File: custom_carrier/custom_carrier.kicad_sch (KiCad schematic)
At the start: 20 parts, among them J1 ERF5-040-05.0-X-DV, J13 PJ-002AH-SMT-TR, J14 87832-1420, J2 ERF5-040-05.0-X-DV, J3 ERF5-040-05.0-X-DV, J4 ERF5-040-05.0-X-DV, J5 45230-220230, J6 45230-220230

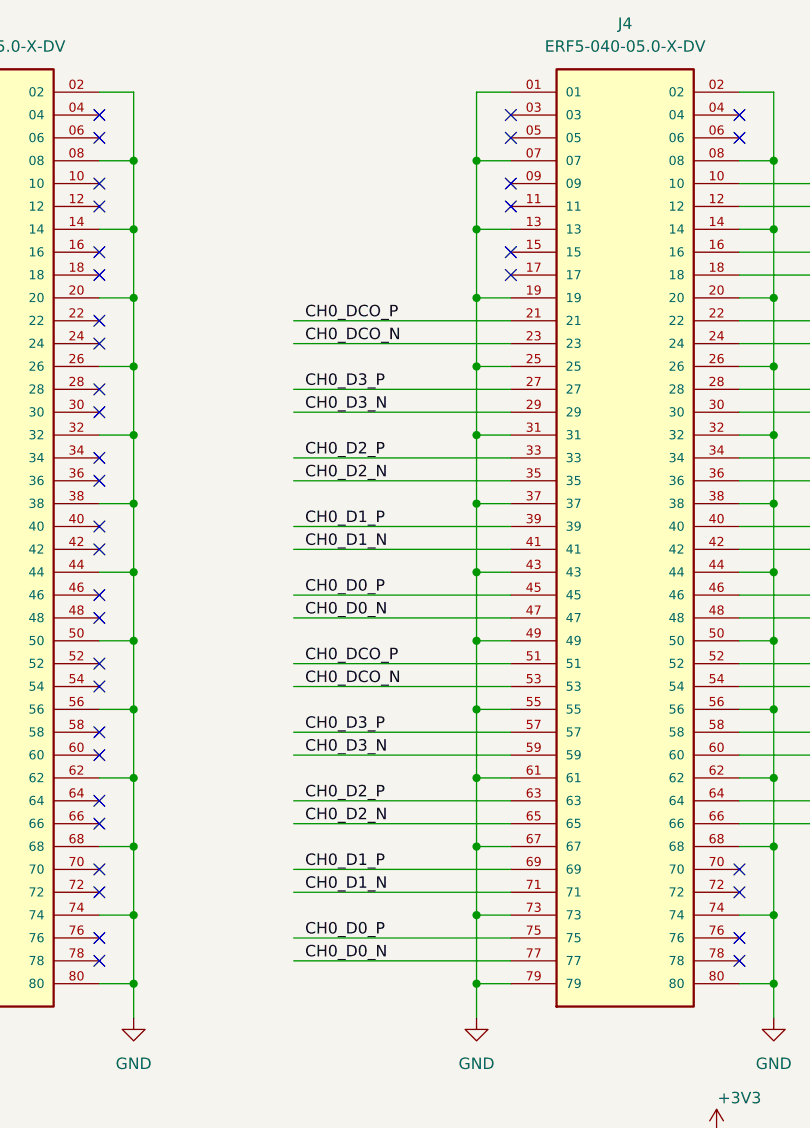
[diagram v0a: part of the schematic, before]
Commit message: fixed loopback wiring error, increased Revision from A-1 to B-1
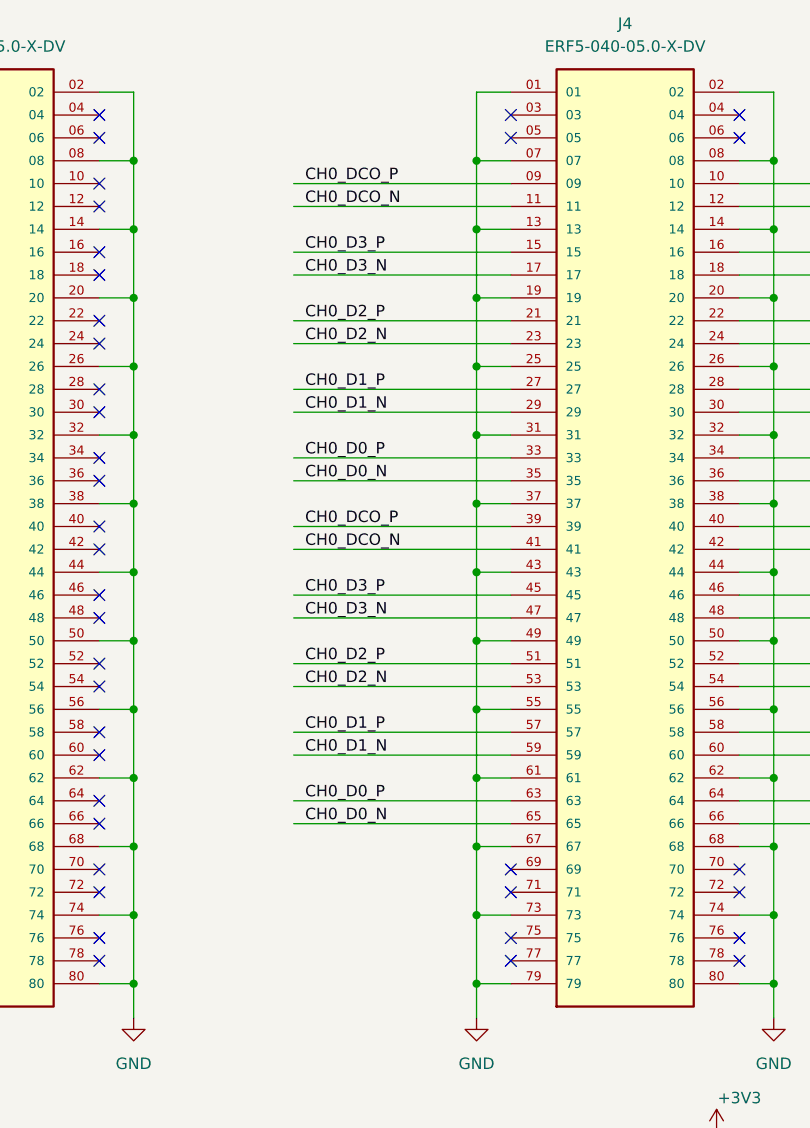
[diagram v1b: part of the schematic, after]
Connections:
- net CH0_D0_N: now also J4.35, J4.65; no longer J4.47, J4.77
- net CH0_D0_P: now also J4.33, J4.63; no longer J4.45, J4.75
- net CH0_D1_N: now also J4.29, J4.59; no longer J4.41, J4.71
- net CH0_D1_P: now also J4.27, J4.57; no longer J4.39, J4.69
- net CH0_D2_N: now also J4.23, J4.53; no longer J4.35, J4.65
- net CH0_D2_P: now also J4.21, J4.51; no longer J4.33, J4.63
- net CH0_D3_N: now also J4.17, J4.47; no longer J4.29, J4.59
- net CH0_D3_P: now also J4.15, J4.45; no longer J4.27, J4.57
- net CH0_DCO_N: now also J4.11, J4.41; no longer J4.23, J4.53
- net CH0_DCO_P: now also J4.09, J4.39; no longer J4.21, J4.51

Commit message: Rev B-1 with proper loopback pinout routed
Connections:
- net CH0_DCO_N: now also J4.71; no longer J4.11
- net CH0_DCO_P: now also J4.69; no longer J4.09
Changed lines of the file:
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@@
 	)
 	(no_connect
+		(at 213.36 34.29)
+	)
+	(no_connect
 		(at 91.44 74.93)
 	)
@@
 	)
 	(no_connect
+		(at 213.36 31.75)
+	)
+	(no_connect
 		(at 116.84 44.45)
 	)
@@
 	)
 	(no_connect
-		(at 213.36 107.95)
-	)
-	(no_connect
 		(at 167.64 39.37)
 	)
@@
 	)
 	(no_connect
-		(at 213.36 110.49)
-	)
-	(no_connect
 		(at 167.64 31.75)
 	)
@@
 	(wire
 		(pts
-			(xy 189.23 69.85) (xy 213.36 69.85)
-		)
-		(stroke
-			(width 0)
-			(type default)
-		)
-	)
-	(wire
-		(pts
 			(xy 104.14 171.45) (xy 104.14 176.53)
 		)
@@
 	(wire
 		(pts
+			(xy 189.23 72.39) (xy 213.36 72.39)
+		)
+		(stroke
+			(width 0)
+			(type default)
+		)
+	)
+	(wire
+		(pts
 			(xy 238.76 85.09) (xy 262.89 85.09)
 		)
@@
 	(wire
 		(pts
+			(xy 189.23 69.85) (xy 213.36 69.85)
+		)
+		(stroke
+			(width 0)
+			(type default)
+		)
+	)
+	(wire
+		(pts
 			(xy 91.44 97.79) (xy 87.63 97.79)
 		)
@@
 	(wire
 		(pts
+			(xy 189.23 107.95) (xy 213.36 107.95)
+		)
+		(stroke
+			(width 0)
+			(type default)
+		)
+	)
+	(wire
+		(pts
 			(xy 54.61 100.33) (xy 63.5 100.33)
 		)
@@
 	(wire
 		(pts
-			(xy 189.23 31.75) (xy 213.36 31.75)
-		)
-		(stroke
-			(width 0)
-			(type default)
-		)
-	)
-	(wire
-		(pts
 			(xy 220.98 149.86) (xy 220.98 157.48)
 		)
@@
 	(wire
 		(pts
-			(xy 17.78 163.83) (xy 36.83 163.83)
+			(xy 189.23 110.49) (xy 213.36 110.49)
 		)
 		(stroke
@@
 	(wire
 		(pts
-			(xy 91.44 21.59) (xy 87.63 21.59)
+			(xy 17.78 163.83) (xy 36.83 163.83)
 		)
 		(stroke
@@
 	(wire
 		(pts
-			(xy 58.42 21.59) (xy 54.61 21.59)
+			(xy 91.44 21.59) (xy 87.63 21.59)
 		)
 		(stroke
@@
 	(wire
 		(pts
-			(xy 242.57 44.45) (xy 242.57 52.07)
+			(xy 58.42 21.59) (xy 54.61 21.59)
 		)
 		(stroke
@@
 	(wire
 		(pts
-			(xy 104.14 180.34) (xy 104.14 182.88)
+			(xy 242.57 44.45) (xy 242.57 52.07)
 		)
 		(stroke
@@
 	(wire
 		(pts
-			(xy 63.5 146.05) (xy 63.5 140.97)
+			(xy 104.14 180.34) (xy 104.14 182.88)
 		)
 		(stroke
@@
 	(wire
 		(pts
-			(xy 167.64 82.55) (xy 171.45 82.55)
+			(xy 63.5 146.05) (xy 63.5 140.97)
 		)
 		(stroke
@@
 	(wire
 		(pts
-			(xy 189.23 72.39) (xy 213.36 72.39)
+			(xy 167.64 82.55) (xy 171.45 82.55)
 		)
 		(stroke
@@
 	(wire
 		(pts
-			(xy 189.23 34.29) (xy 213.36 34.29)
-		)
-		(stroke
-			(width 0)
-			(type default)
-		)
-	)
-	(wire
-		(pts
 			(xy 238.76 80.01) (xy 262.89 80.01)
 		)
@@
 		)
 	)
-	(label "CH0_DCO_P"
-		(at 190.5 31.75 0)
-		(fields_autoplaced yes)
-		(effects
-			(font
-				(size 1.27 1.27)
-			)
-			(justify left bottom)
-		)
-	)
 	(label "CH1_CLK_N"
 		(at 250.19 102.87 0)
@@
 		)
 	)
-	(label "CH0_DCO_P"
-		(at 190.5 69.85 0)
-		(fields_autoplaced yes)
-		(effects
-			(font
-				(size 1.27 1.27)
-			)
-			(justify left bottom)
-		)
-	)
 	(label "CH1_RX2_N"
 		(at 251.46 41.91 0)
@@
 		)
 	)
-	(label "JTAG_TDO"
-		(at 200.66 154.94 0)
+	(label "CH0_DCO_N"
+		(at 190.5 72.39 0)
 		(fields_autoplaced yes)
 		(effects
@@
 		)
 	)
-	(label "CH0_DCO_N"
-		(at 190.5 72.39 0)
+	(label "JTAG_TDO"
+		(at 200.66 154.94 0)
 		(fields_autoplaced yes)
 		(effects
@@
 		)
 	)
+	(label "CH0_DCO_N"
+		(at 190.5 110.49 0)
+		(fields_autoplaced yes)
+		(effects
+			(font
+				(size 1.27 1.27)
+			)
+			(justify left bottom)
+		)
+	)
 	(label "CH0_D2_N"
 		(at 190.5 87.63 0)
@@
 		)
 	)
+	(label "CH0_DCO_P"
+		(at 190.5 69.85 0)
+		(fields_autoplaced yes)
+		(effects
+			(font
+				(size 1.27 1.27)
+			)
+			(justify left bottom)
+		)
+	)
 	(label "CH0_D1_P"
 		(at 190.5 54.61 0)
@@
 		)
 	)
-	(label "CH1_DCO_P"
-		(at 67.31 143.51 0)
+	(label "CH0_DCO_P"
+		(at 190.5 107.95 0)
 		(fields_autoplaced yes)
 		(effects
@@
 		)
 	)
-	(label "CH1_CLK_P"
-		(at 138.43 143.51 0)
+	(label "CH1_DCO_P"
+		(at 67.31 143.51 0)
 		(fields_autoplaced yes)
 		(effects
@@
 		)
 	)
-	(label "CH1_RX1_N"
-		(at 19.05 153.67 0)
+	(label "CH1_CLK_P"
+		(at 138.43 143.51 0)
 		(fields_autoplaced yes)
 		(effects
@@
 		)
 	)
-	(label "CH0_DCO_N"
-		(at 190.5 34.29 0)
+	(label "CH1_RX1_N"
+		(at 19.05 153.67 0)
 		(fields_autoplaced yes)
 		(effects

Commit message: added annotation to schematic for J3 that really isn't needed
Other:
- note added: "Not Required"
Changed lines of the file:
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@@
+		)
+	)
+	(text "Not Required"
+		(exclude_from_sim no)
+		(at 155.194 129.032 0)
+		(effects
+			(font
+				(size 2.54 2.54)
+				(thickness 0.508)
+				(bold yes)
+			)
 		)
 	)
